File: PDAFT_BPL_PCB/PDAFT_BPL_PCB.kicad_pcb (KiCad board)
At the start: 2 copper layers, 63.4 x 85.5 mm, 19 parts

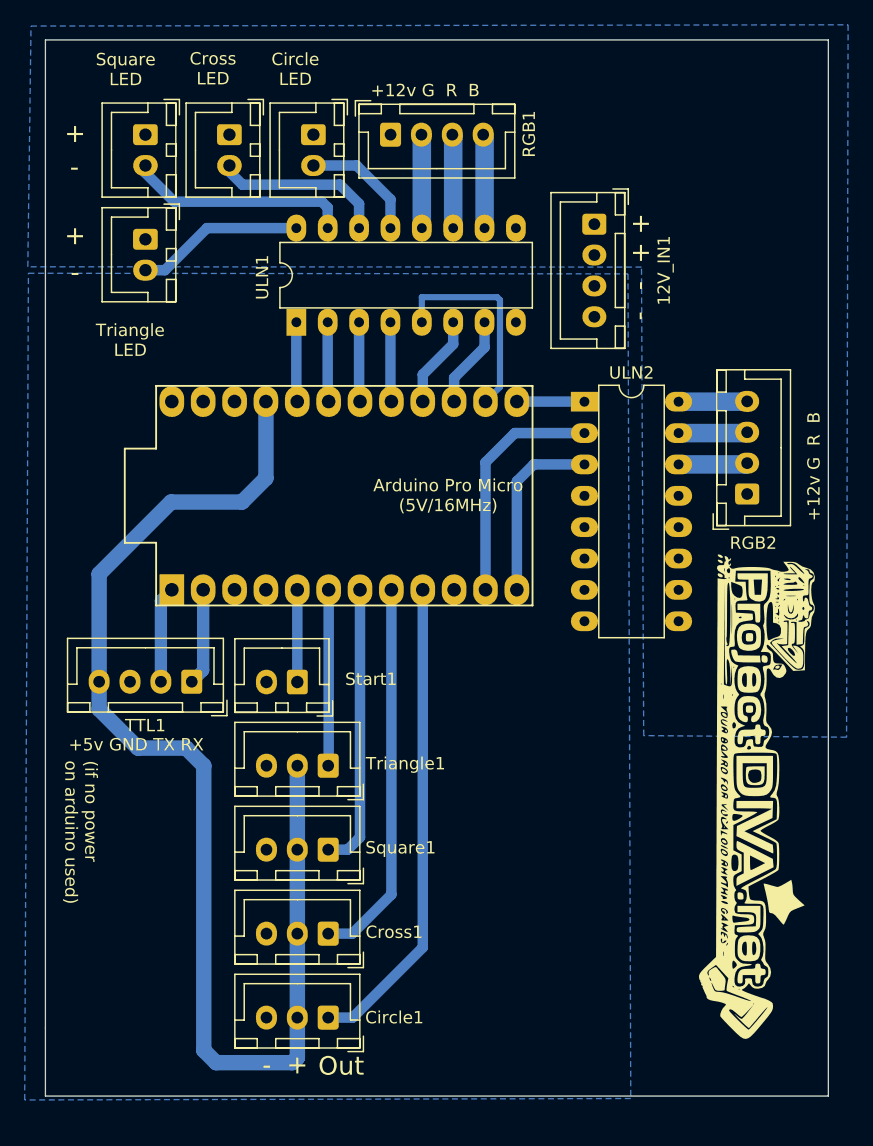
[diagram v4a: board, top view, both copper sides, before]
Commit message: Firmware update
Firmware updated (USB-Serial and serial1 different firmware files), added 3D-model of Arduino for picture, pictures added, readme updated
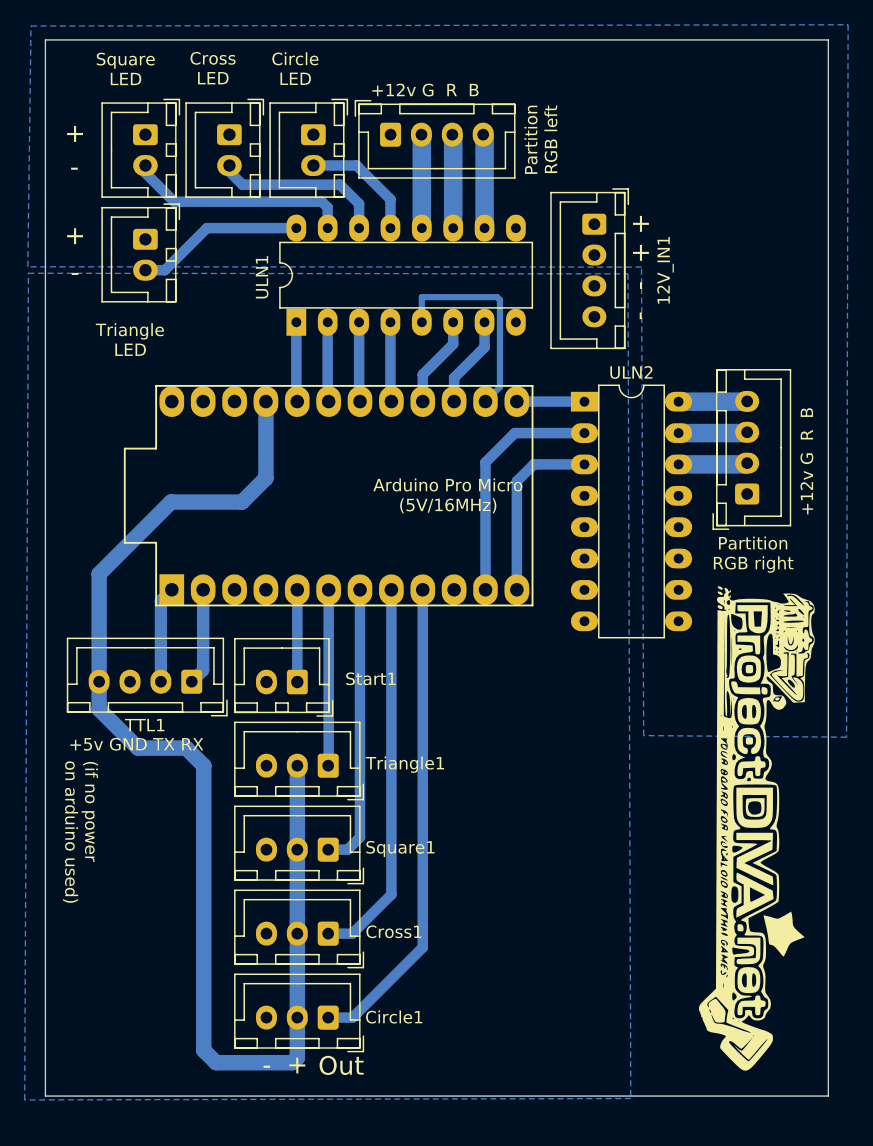
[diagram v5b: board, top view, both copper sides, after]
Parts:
- moved G*** 2.58 mm to (159.1, 94.4)
- renumbered RGB1 to Partition_L1, RGB2 to Partition_R1
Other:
- board text added: "B R G +12v"
- board text added: "Partition RGB left"
- board text added: "Partition RGB right"

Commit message: PCB update
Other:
- board text added: "TTL"
- board text added: "UNL2003"
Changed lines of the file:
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@@
     (property "Sheetname" "")
     (attr through_hole)
-    (fp_text reference "Circle1" (at -5.365 0) (layer "F.SilkS")
+    (fp_text reference "Circle1" (at -5.365 0) (layer "F.SilkS") hide
       (effects (font (size 1 1) (thickness 0.15)))
     )
@@
     (property "Sheetname" "")
     (attr through_hole)
-    (fp_text reference "Cross1" (at -5.346958 0.115477) (layer "F.SilkS")
+    (fp_text reference "Cross1" (at -5.346958 0.115477) (layer "F.SilkS") hide
       (effects (font (size 1 1) (thickness 0.15)))
     )
@@
     (property "Sheetname" "")
     (attr through_hole)
-    (fp_text reference "Square1" (at -5.866927 0.155647) (layer "F.SilkS")
+    (fp_text reference "Square1" (at -5.866927 0.155647) (layer "F.SilkS") hide
       (effects (font (size 1 1) (thickness 0.15)))
     )
@@
     (property "Sheetname" "")
     (attr through_hole)
-    (fp_text reference "Triangle1" (at -6.274552 0.166653) (layer "F.SilkS")
+    (fp_text reference "Triangle1" (at -6.274552 0.166653) (layer "F.SilkS") hide
       (effects (font (size 1 1) (thickness 0.15)))
     )
@@
     (property "Sheetname" "")
     (attr through_hole)
-    (fp_text reference "Start1" (at -5.975 0.225 180) (layer "F.SilkS")
+    (fp_text reference "Start1" (at -5.975 0.225 180) (layer "F.SilkS") hide
       (effects (font (size 1 1) (thickness 0.15)))
     )
@@
     (property "Sheetname" "")
     (attr through_hole)
-    (fp_text reference "ULN1" (at 3.64 -2.745 270) (layer "F.SilkS")
+    (fp_text reference "ULN1" (at 3.64 -2.745 270) (layer "F.SilkS") hide
       (effects (font (size 1 1) (thickness 0.15)))
     )
@@
     (property "Sheetname" "")
     (attr through_hole)
-    (fp_text reference "ULN2" (at 3.81 -2.33) (layer "F.SilkS")
+    (fp_text reference "ULN2" (at 3.81 -2.33) (layer "F.SilkS") hide
       (effects (font (size 1 1) (thickness 0.15)))
     )
@@
     (property "Sheetname" "")
     (attr through_hole)
-    (fp_text reference "TTL1" (at 3.75 -3.55) (layer "F.SilkS")
+    (fp_text reference "TTL1" (at 3.75 -3.55) (layer "F.SilkS") hide
       (effects (font (size 1 1) (thickness 0.15)))
     )
@@
     (effects (font (size 1 1) (thickness 0.25)) (justify mirror))
   )
-  (gr_text "Square" (at 129.875 96.3) (layer "B.SilkS")
+  (gr_text "Square" (at 130.275 96.1) (layer "B.SilkS")
     (effects (font (size 1 1) (thickness 0.25)) (justify mirror))
   )
-  (gr_text "Cross \nLED" (at 115.025 32.8) (layer "B.SilkS")
+  (gr_text "Cross \nLED" (at 116.6 32.9) (layer "B.SilkS")
     (effects (font (size 1 1) (thickness 0.25)) (justify mirror))
   )
@@
     (effects (font (size 1.3 1.3) (thickness 0.2)) (justify mirror))
   )
-  (gr_text "Circle \nLED" (at 121.775 32.8) (layer "B.SilkS")
+  (gr_text "Circle \nLED" (at 123.1 32.95) (layer "B.SilkS")
     (effects (font (size 1 1) (thickness 0.25)) (justify mirror))
   )
@@
     (effects (font (size 1 1) (thickness 0.15)) (justify mirror))
   )
-  (gr_text "Triangle \nLED" (at 108.32 54.79) (layer "B.SilkS")
+  (gr_text "Triangle \nLED" (at 109.175 54.575) (layer "B.SilkS")
     (effects (font (size 1 1) (thickness 0.25)) (justify mirror))
   )
@@
     (effects (font (size 1.5 1.5) (thickness 0.3)))
   )
-  (gr_text "Cross" (at 129.38 103.42) (layer "B.SilkS")
+  (gr_text "Cross" (at 129.825 102.825) (layer "B.SilkS")
     (effects (font (size 1 1) (thickness 0.25)) (justify mirror))
   )
-  (gr_text "Circle" (at 129.38 110.53) (layer "B.SilkS")
+  (gr_text "Circle" (at 130.05 109.175) (layer "B.SilkS")
     (effects (font (size 1 1) (thickness 0.25)) (justify mirror))
   )
-  (gr_text "Square \nLED" (at 108.075 32.865) (layer "B.SilkS")
+  (gr_text "Square \nLED" (at 109.625 32.925) (layer "B.SilkS")
     (effects (font (size 1 1) (thickness 0.25)) (justify mirror))
   )
@@
     (effects (font (size 1 1) (thickness 0.15)) (justify mirror))
   )
-  (gr_text "Circle \nLED" (at 121.84 32.86) (layer "F.SilkS")
+  (gr_text "Circle \nLED" (at 123.275 32.95) (layer "F.SilkS")
     (effects (font (size 1 1) (thickness 0.25)))
   )
-  (gr_text "Cross \nLED" (at 115.17 32.81) (layer "F.SilkS")
+  (gr_text "Cross \nLED" (at 116.5 32.925) (layer "F.SilkS")
     (effects (font (size 1 1) (thickness 0.25)))
   )
-  (gr_text "Square \nLED" (at 108.1 32.875) (layer "F.SilkS")
+  (gr_text "Square \nLED" (at 109.85 32.925) (layer "F.SilkS")
     (effects (font (size 1 1) (thickness 0.25)))
   )
-  (gr_text "Triangle \nLED" (at 108.475 54.8) (layer "F.SilkS")
+  (gr_text "Triangle \nLED" (at 109.675 54.025) (layer "F.SilkS")
     (effects (font (size 1 1) (thickness 0.25)))
   )
@@
     (effects (font (size 1 1) (thickness 0.25)))
   )
+  (gr_text "Start" (at 127.7 82.35) (layer "F.SilkS")
+    (effects (font (size 1 1) (thickness 0.25)))
+  )
   (gr_text "(if no power \non arduino used)" (at 104.475 88.825 270) (layer "F.SilkS")
     (effects (font (size 1 1) (thickness 0.15)) (justify left))
   )
+  (gr_text "UNL2003" (at 148.875 57.175) (layer "F.SilkS")
+    (effects (font (size 1 1) (thickness 0.25)))
+  )
   (gr_text "+" (at 104 46.325) (layer "F.SilkS")
     (effects (font (size 1.5 1.5) (thickness 0.3)) (justify mirror))
   )
+  (gr_text "Circle" (at 130.025 109.225) (layer "F.SilkS")
+    (effects (font (size 1 1) (thickness 0.25)))
+  )
   (gr_text "+" (at 149.825 45.325) (layer "F.SilkS")
     (effects (font (size 1.5 1.5) (thickness 0.3)) (justify mirror))
@@
     (effects (font (size 1.5 1.5) (thickness 0.3)))
   )
+  (gr_text "TTL" (at 109.65 85.975) (layer "F.SilkS")
+    (effects (font (size 1 1) (thickness 0.25)))
+  )
+  (gr_text "Triangle" (at 130.725 89.125) (layer "F.SilkS")
+    (effects (font (size 1 1) (thickness 0.25)))
+  )
+  (gr_text "UNL2003" (at 119.4 49.75 90) (layer "F.SilkS")
+    (effects (font (size 1 1) (thickness 0.25)))
+  )
   (gr_text "+12v G  R  B" (at 132.35 34.575) (layer "F.SilkS")
     (effects (font (size 1 1) (thickness 0.15)))
   )
+  (gr_text "Cross" (at 129.825 102.9) (layer "F.SilkS")
+    (effects (font (size 1 1) (thickness 0.25)))
+  )
   (gr_text "-" (at 104 49.3) (layer "F.SilkS")
     (effects (font (size 1.5 1.5) (thickness 0.3)))
@@
     (effects (font (size 1 1) (thickness 0.2)))
   )
+  (gr_text "Square" (at 130.3 96.025) (layer "F.SilkS")
+    (effects (font (size 1 1) (thickness 0.25)))
+  )
   (segment (start 121.79 74.8) (end 121.995001 75.005001) (width 0.85) (layer "B.Cu") (net 1))

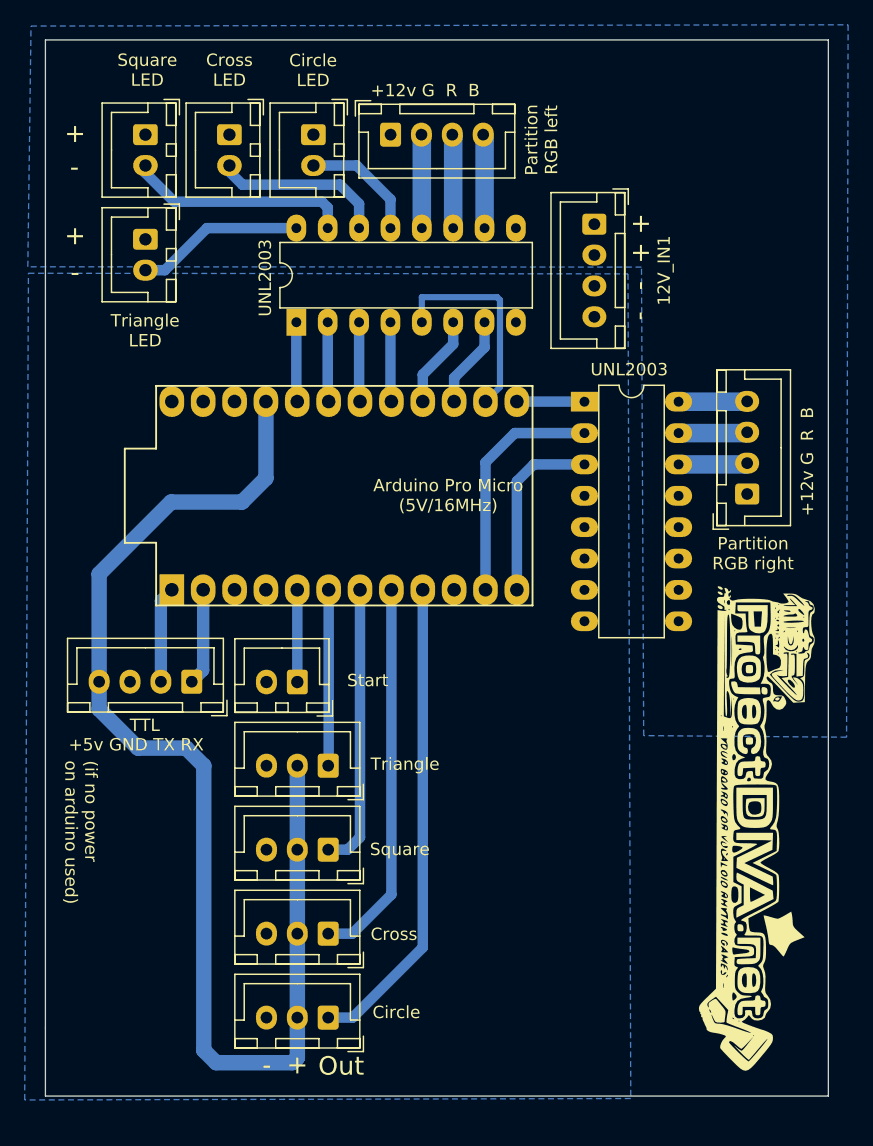
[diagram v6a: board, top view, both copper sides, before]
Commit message: Additional poligon on the top, other fixes
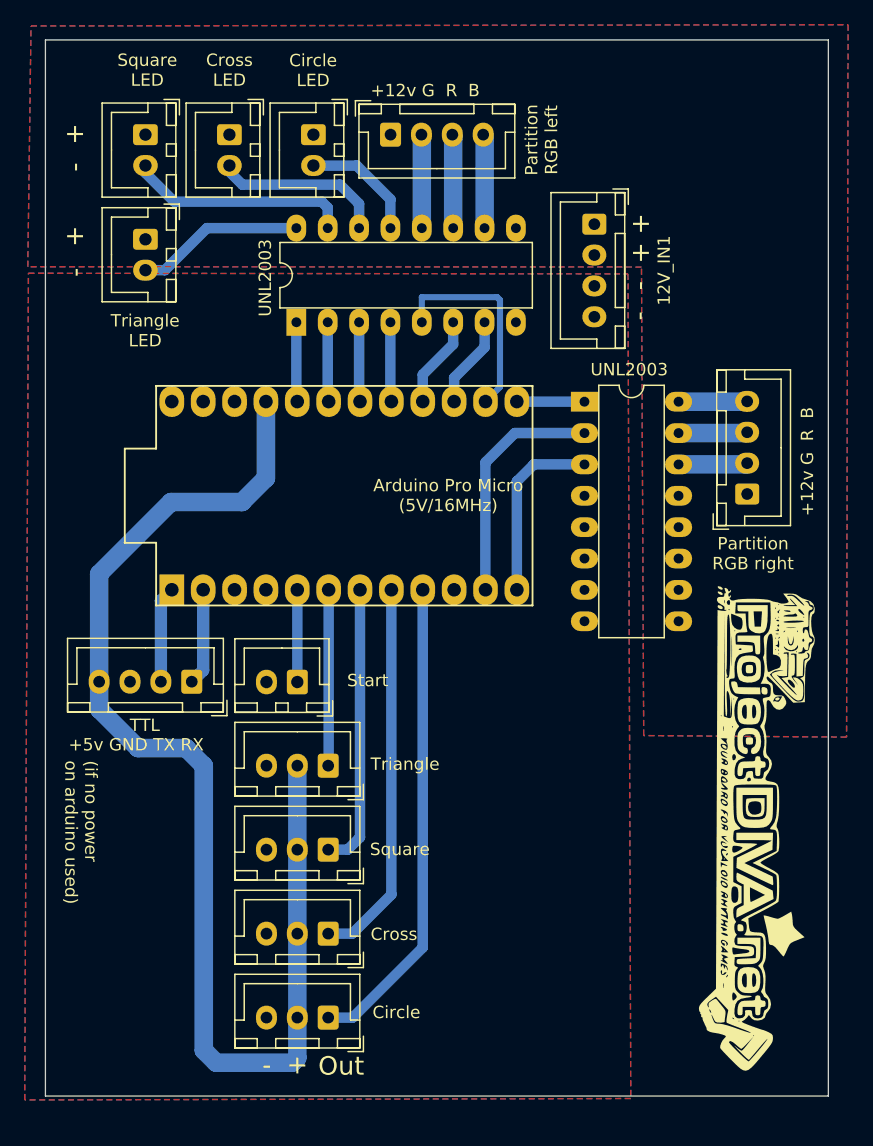
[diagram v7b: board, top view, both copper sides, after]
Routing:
- added copper zone on F.Cu, net Net-(12V_IN1-Pad1)
- added copper zone on F.Cu, net Net-(12V_IN1-Pad3)
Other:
- outline, holes or cut-outs redrawn
